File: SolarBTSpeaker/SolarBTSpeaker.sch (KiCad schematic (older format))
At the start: 27 parts

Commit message: Schematic updated
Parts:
- removed U?: LM2623AMM_NOPB, MUA08A, symbol LM2623:LM2623AMM_NOPB
- added C1, C10, C12, C16, C18: 0.1u, symbol Device:C_Small
- added C11, C13, C14, C17, C23, C24, C31, C32, C6, C7: 1000p, symbol Device:C_Small
- added C15, C9: 100u, symbol Device:CP1_Small
- added C19, C21, C25, C27: 0.22u, symbol Device:C_Small
- added C20, C22, C26, C29, C30, C33: 1u, symbol Device:C_Small
- added C28: 300u, symbol Device:CP1_Small
- added C8: 68u, symbol Device:CP1_Small
- added D4: 1N5822, Diode_THT:D_DO-201AD_P15.24mm_Horizontal, symbol Diode:1N5822
- added FB1, FB2, FB3, FB4: Ferrite_Bead_Small, symbol Device:Ferrite_Bead_Small
- added J10: IN_LEFT-, symbol Connector_Generic:Conn_01x01
- added J11: OUT_RIGHT-, symbol Connector_Generic:Conn_01x01
- added J12: IN_RIGHT-, symbol Connector_Generic:Conn_01x01
- added J13: OUT_RIGHT+, symbol Connector_Generic:Conn_01x01
- added J14: IN_RIGHT+, symbol Connector_Generic:Conn_01x01
- added J15: GAIN_Jumper, symbol Connector_Generic:Conn_01x03
- added J16, J17: Conn_01x01, symbol Connector_Generic:Conn_01x01
- added J7: OUT_LEFT+, symbol Connector_Generic:Conn_01x01
- added J8: OUT_LEFT-, symbol Connector_Generic:Conn_01x01
- added J9: IN_LEFT+, symbol Connector_Generic:Conn_01x01
- added L1: 22u, symbol Device:L
- added R1: 330, symbol Device:R_Small_US
- added R10, R11, R14, R9: 68, symbol Device:R_Small_US
- added R12, R13: 100k, symbol Device:R_Small_US
- added R15: 39k, symbol Device:R_Small_US
- added R2, R6: 5.1M, symbol Device:R_Small_US
- added R3: 2.2k, symbol Device:R_Small_US
- added Rsense1: 20m, symbol Device:R_Small_US
- added SW2: SW_SPDT, symbol Switch:SW_SPDT
- added TP4, TP5, TP6: TestPoint, symbol Connector:TestPoint
- added U3, U4: CSD16404Q5A, DQJ8, symbol CSD16404Q5A:CSD16404Q5A
- added U5: SIRA18ADP, symbol SolarBTSpeakerLib:SIRA18ADP
- added U6: max1771cpa+, 21-0043D_8, symbol MAX1771CPA+:max1771cpa+
- Rtherm1: renamed from R?; value 1M -> 21.5k
- SW1: renamed from SW?; value SW_DPDT_x2 -> SW_Input
- gave numbers to parts that had none: 23
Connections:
- net GND: now also U7.14 (AGND), U7.19 (GND), U7.24 (GND), U7.29 (PAD), U7.6 (MODE_SEL), U7.8 (GND), C10.2, C11.2, C12.2, C13.2, C15.2, C16.2, C17.2, C18.2, C20.2, C23.2, C28.2, C31.2, C33.2, C6.2, C8.2, C9.2, J15.1 (Pin_1), R10.2, R11.2, R14.2, R15.1, R3.2, R6.2, R9.2, Rsense1.2, U4.1 (S), U6.3 (FB), U6.4 (SHDN), U6.6 (AGND), U6.7 (GND)
- net at U7.10 (PLIMIT): now also U7.9 (GVDD), C33.1, R15.2
- net at U7.11 (RINN): now also C29.1
- net at U7.12 (RINP): now also C30.1
- net +12V: now reaches U7.15 (PVCC)
- net +12V: now also U7.16 (PVCC), U7.27 (PVCC), U7.28 (PVCC), U7.7 (AVCC), C10.1, C11.1, C12.1, C15.1, C16.1, C17.1, C20.1, C28.1, C9.1, D4.1 (K), R12.2, R13.2, TP4.1, TP5.1, TP6.1, U6.2 (V+)
- net at U7.17 (BSPR): now also C27.2
- net at U7.18 (OUTPR): now also C27.1, FB4.2
- net at U7.2 (SDZ_FAULT_N): now also R12.1
- net at U7.20 (OUTNR): now also C25.1, FB3.2
- net at U7.21 (BSNR): now also C25.2
- net at U7.22 (BSNL): now also C21.2
- net at U7.23 (OUTNL): now also C21.1, FB2.2
- net at U7.25 (OUTPL): now also C19.1, FB1.2
- net at U7.26 (BSPL): now also C19.2
- net at U7.3 (LINP): now also C22.1
- net at U7.4 (LINN): now also C26.1
- net at U7.5 (GAIN_SEL): now also J15.2 (Pin_2)
- net at U2.2 (COUT): now also R6.1, U4.2 (G)
- net at U2.3 (DOUT): now also R2.1, U3.2 (G)
- net at U2.4 (VSS): now also C1.2, J17.1 (Pin_1), R2.2, U3.1 (S)
- net at U2.5 (BAT): now also C1.1, R1.2
- net at U2.6 (V-): now also R3.1
- net BAT+: now reaches C4.1, C5.1, TP3.1, U1.10 (BAT)
- net BAT+: now also R7.2, R8.2, J16.1 (Pin_1), R1.1, SW2.2 (B)
- new net: U3.3 (D), U4.3 (D)
- new net: U5.4 (G), U6.1 (EXT)
- new net: C18.1, U6.5 (REF)
- new net: Rsense1.1, U5.1 (S), U5.2 (S), U5.3 (S), U6.8 (CS)
- new net: C8.1, L1.1, SW2.1 (A)
- new net: D4.2 (A), L1.2, U5.5 (D)
- new net: C22.2, J9.1 (Pin_1)
- new net: C26.2, J10.1 (Pin_1)
- new net: C29.2, J12.1 (Pin_1)
- new net: C30.2, J14.1 (Pin_1)
- new net: C6.1, C7.1, FB1.1, J7.1 (Pin_1)
- new net: C7.2, R9.1
- new net: C13.1, C14.1, FB2.1, J8.1 (Pin_1)
- new net: C14.2, R10.1
- new net: C23.1, C24.1, FB3.1, J11.1 (Pin_1)
- new net: C24.2, R11.1
- new net: C31.1, C32.1, FB4.1, J13.1 (Pin_1)
- new net: C32.2, R14.1
- new net: J15.3 (Pin_3), R13.1
- no-connect marks 1 -> 4
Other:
- note added: "Amplifier"
- note added: "Batt Input"
- note added: "Battery Charger"
- note added: "Battery Protection"
- note added: "DC-DC Boost Controller (12V Output)"
- note added: "Vin"
- note added: "Vout"
- moved on the sheet: C2, C3, C4, C5, D1, D2, D3, J1, J2, J3, J4, J5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

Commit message: Minor schematic updates
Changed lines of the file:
@@
 Connection ~ 6850 1300
 Wire Wire Line
-	7300 1300 7650 1300
+	7300 1300 7350 1300
 Connection ~ 7300 1300
 Wire Wire Line
@@
 Wire Notes Line
 	1800 7100 6700 7100
+Connection ~ 7350 1300
+Wire Wire Line
+	7350 1300 7650 1300
 $EndSCHEMATC

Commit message: Schematic Update
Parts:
- removed D1: D_Schottky, symbol Device:D_Schottky
- added C29: 150u, symbol Device:CP1_Small
- added D1: 1N5822, Diode_THT:D_DO-201AD_P15.24mm_Horizontal, symbol Diode:1N5822
- C1, C10, C11, C12, C13, C14, C16, C17, C18, C19, C2, C20, C21, C22, C23, C24, C25, C26, C27, C3, C4, C5, C6, C7: footprint (none) -> Capacitor_SMD:C_0805_2012Metric_Pad1.15x1.40mm_HandSolder
- C15, C8, C9: footprint (none) -> Capacitor_THT:CP_Radial_D6.3mm_P2.50mm
- C28: value 300u -> 150u
- C30: renamed from C29; footprint (none) -> Capacitor_SMD:C_0805_2012Metric_Pad1.15x1.40mm_HandSolder
- C31: renamed from C30; footprint (none) -> Capacitor_SMD:C_0805_2012Metric_Pad1.15x1.40mm_HandSolder
- C32: renamed from C31; footprint (none) -> Capacitor_SMD:C_0805_2012Metric_Pad1.15x1.40mm_HandSolder
- C33: renamed from C32; footprint (none) -> Capacitor_SMD:C_0805_2012Metric_Pad1.15x1.40mm_HandSolder
- C34: renamed from C33; footprint (none) -> Capacitor_SMD:C_0805_2012Metric_Pad1.15x1.40mm_HandSolder
- FB1, FB2, FB3, FB4, R1, R10, R11, R12, R13, R14, R15, R2, R3, R4, R5, R6, R7, R8, R9, Rsense1, Rtherm1: footprint (none) -> Resistor_SMD:R_0805_2012Metric_Pad1.15x1.40mm_HandSolder
- J1: renamed from J16; footprint (none) -> Connector_Wire:SolderWirePad_1x01_Drill1.5mm
- J10: renamed from J8; footprint (none) -> Connector_Wire:SolderWirePad_1x01_Drill1.5mm
- J11: renamed from J9; footprint (none) -> Connector_Wire:SolderWirePad_1x01_Drill1.5mm
- J12: renamed from J10; footprint (none) -> Connector_Wire:SolderWirePad_1x01_Drill1.5mm
- J13: renamed from J11; footprint (none) -> Connector_Wire:SolderWirePad_1x01_Drill1.5mm
- J14: renamed from J12; footprint (none) -> Connector_Wire:SolderWirePad_1x01_Drill1.5mm
- J15: renamed from J13; footprint (none) -> Connector_Wire:SolderWirePad_1x01_Drill1.5mm
- J16: renamed from J14; footprint (none) -> Connector_Wire:SolderWirePad_1x01_Drill1.5mm
- J17: renamed from J15; footprint (none) -> Connector_PinSocket_2.54mm:PinSocket_1x03_P2.54mm_Vertical
- J2: renamed from J17; footprint (none) -> Connector_Wire:SolderWirePad_1x01_Drill1.5mm
- J3: renamed from J1; footprint (none) -> Connector_Wire:SolderWirePad_1x01_Drill1.5mm
- J4: renamed from J2; footprint (none) -> Connector_Wire:SolderWirePad_1x01_Drill1.5mm
- J5: renamed from J3; footprint (none) -> Connector_Wire:SolderWirePad_1x01_Drill1.5mm
- J6: renamed from J4; footprint (none) -> Connector_Wire:SolderWirePad_1x01_Drill1.5mm
- J7: renamed from J5; footprint (none) -> Connector_Wire:SolderWirePad_1x01_Drill1.5mm
- J8: renamed from J6; footprint (none) -> Connector_Wire:SolderWirePad_1x01_Drill1.5mm
- J9: renamed from J7; footprint (none) -> Connector_Wire:SolderWirePad_1x01_Drill1.5mm
- SW1: footprint (none) -> Button_Switch_THT:SW_CuK_JS202011CQN_DPDT_Straight
- TP1, TP2, TP3, TP4, TP5, TP6: footprint (none) -> TestPoint:TestPoint_Pad_D1.0mm
- U1: footprint DQC10_P84X2P4 -> Package_SON:WSON-10-1EP_2x3mm_P0.5mm_EP0.84x2.4mm
- U2: footprint DSE0006A -> Package_SON:WSON-6_1.5x1.5mm_P0.5mm
- U3, U4: footprint DQJ8 -> Package_SON:VSONP-8-1EP_5x6_P1.27mm
- U5: footprint (none) -> Package_SO:PowerPAK_SO-8_Single
- U6: value max1771cpa+ -> max1771csa+; footprint 21-0043D_8 -> Package_SO:SOIC-8_3.9x4.9mm_P1.27mm
- U7: footprint PWP0028H_N -> Package_SO:HTSSOP-28-1EP_4.4x9.7mm_P0.65mm_EP2.85x5.4mm
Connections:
- net +12V: now also C29.1
- net GND: now also C29.2
- net at J3.1 (Pin_1): now also D1.2 (A)
- net at SW1.3 (C): now also D1.1 (K)

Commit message: Updated schematic with datasheets, fixed ERC warnings
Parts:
- C28, C29: footprint (none) -> Capacitor_THT:CP_Radial_D6.3mm_P2.50mm
- D2, D3: footprint (none) -> LED_THT:LED_D3.0mm
- L1: footprint (none) -> Solar BT Speaker Footprints:L_Radial_D14.8mm_P12mm_Wurth
- SW2: footprint (none) -> Connector_PinSocket_2.54mm:PinSocket_1x03_P2.54mm_Vertical
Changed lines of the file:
@@
 F 0 "D2" V 6197 3228 50  0000 L CNN
 F 1 "LED" V 6288 3228 50  0000 L CNN
-F 2 "" H 6250 3150 50  0001 C CNN
+F 2 "LED_THT:LED_D3.0mm" H 6250 3150 50  0001 C CNN
 F 3 "~" H 6250 3150 50  0001 C CNN
 	1    6250 3150
@@
 F 0 "D3" V 6597 3228 50  0000 L CNN
 F 1 "LED" V 6688 3228 50  0000 L CNN
-F 2 "" H 6650 3150 50  0001 C CNN
+F 2 "LED_THT:LED_D3.0mm" H 6650 3150 50  0001 C CNN
 F 3 "~" H 6650 3150 50  0001 C CNN
 	1    6650 3150
@@
 F 1 "CSD16404Q5A" H 10450 3251 60  0000 C CNN
 F 2 "Package_SON:VSONP-8-1EP_5x6_P1.27mm" H 10450 3240 60  0001 C CNN
-F 3 "" H 9850 3100 60  0000 C CNN
+F 3 "http://www.ti.com/general/docs/suppproductinfo.tsp?distId=10&gotoUrl=http%3A%2F%2Fwww.ti.com%2Flit%2Fgpn%2Fcsd16404q5a" H 10450 3251 60  0001 C CNN
 	1    9550 3100
 	1    0    0    -1
@@
 F 1 "CSD16404Q5A" H 10450 2401 60  0000 C CNN
 F 2 "Package_SON:VSONP-8-1EP_5x6_P1.27mm" H 10450 2390 60  0001 C CNN
-F 3 "" H 9850 2250 60  0000 C CNN
+F 3 "http://www.ti.com/general/docs/suppproductinfo.tsp?distId=10&gotoUrl=http%3A%2F%2Fwww.ti.com%2Flit%2Fgpn%2Fcsd16404q5a" H 9850 2250 60  0001 C CNN
 	1    9550 2250
 	1    0    0    -1
@@
 F 1 "max1771csa+" H 2900 6581 60  0000 C CNN
 F 2 "Package_SO:SOIC-8_3.9x4.9mm_P1.27mm" H 2900 6590 60  0001 C CNN
-F 3 "" H 3550 6100 60  0000 C CNN
+F 3 "https://datasheets.maximintegrated.com/en/ds/MAX1771.pdf" H 2900 6581 60  0001 C CNN
 	1    1800 6050
 	1    0    0    -1
@@
 F 0 "L1" V 5140 4850 50  0000 C CNN
 F 1 "22u" V 5049 4850 50  0000 C CNN
-F 2 "" H 4950 4850 50  0001 C CNN
-F 3 "~" H 4950 4850 50  0001 C CNN
+F 2 "Solar BT Speaker Footprints:L_Radial_D14.8mm_P12mm_Wurth" H 4950 4850 50  0001 C CNN
+F 3 "https://www.we-online.de/katalog/datasheet/744750560220.pdf" H 4950 4850 50  0001 C CNN
 	1    4950 4850
 	0    -1   -1   0
 $EndComp
-$Comp
-L SolarBTSpeakerLib:SIRA18ADP U5
-U 1 1 5EADD78B
-P 3650 5700
-F 0 "U5" H 4550 5957 60  0000 C CNN
-F 1 "SIRA18ADP" H 4550 5851 60  0000 C CNN
-F 2 "Package_SO:PowerPAK_SO-8_Single" H 4550 5840 60  0001 C CNN
-F 3 "" H 3950 5700 60  0000 C CNN
-	1    3650 5700
-	1    0    0    -1
-$EndComp
-Wire Wire Line
-	3950 6000 3550 6000
-Wire Wire Line
-	3950 5700 3950 5800
-Connection ~ 3950 5800
-Wire Wire Line
-	3950 5800 3950 5900
-Wire Wire Line
-	5150 5700 5150 5800
-Connection ~ 5150 5800
-Wire Wire Line
-	5150 5800 5150 5900
-Connection ~ 5150 5900
-Wire Wire Line
-	5150 5900 5150 6000
 Wire Wire Line
 	3950 5900 3700 5900
 Wire Wire Line
 	3700 5900 3700 6300
-Connection ~ 3950 5900
 Wire Wire Line
 	3550 6300 3700 6300
@@
 F 1 "68u" H 4841 5005 50  0000 L CNN
 F 2 "Capacitor_THT:CP_Radial_D6.3mm_P2.50mm" H 4750 5050 50  0001 C CNN
-F 3 "~" H 4750 5050 50  0001 C CNN
+F 3 "https://b2b-api.panasonic.eu/file_stream/pids/fileversion/8157" H 4750 5050 50  0001 C CNN
 	1    4750 5050
 	1    0    0    -1
@@
 F 1 "1N5822" H 5400 5575 50  0000 C CNN
 F 2 "Diode_THT:D_DO-201AD_P15.24mm_Horizontal" H 5400 5525 50  0001 C CNN
-F 3 "http://www.vishay.com/docs/88526/1n5820.pdf" H 5400 5700 50  0001 C CNN
+F 3 "https://www.onsemi.com/pub/Collateral/1N5820-D.PDF" H 5400 5700 50  0001 C CNN
 	1    5400 5700
 	-1   0    0    1
@@
 F 0 "C28" H 4341 6596 50  0000 L CNN
 F 1 "150u" H 4341 6505 50  0000 L CNN
-F 2 "" H 4250 6550 50  0001 C CNN
-F 3 "~" H 4250 6550 50  0001 C CNN
+F 2 "Capacitor_THT:CP_Radial_D6.3mm_P2.50mm" H 4250 6550 50  0001 C CNN
+F 3 "https://www.we-online.de/katalog/datasheet/860020373008.pdf" H 4250 6550 50  0001 C CNN
 	1    4250 6550
 	1    0    0    -1
@@
 F 0 "SW2" H 4350 5235 50  0000 C CNN
 F 1 "SW_SPDT" H 4350 5144 50  0000 C CNN
-F 2 "" H 4350 4950 50  0001 C CNN
+F 2 "Connector_PinSocket_2.54mm:PinSocket_1x03_P2.54mm_Vertical" H 4350 4950 50  0001 C CNN
 F 3 "~" H 4350 4950 50  0001 C CNN
 	1    4350 4950
@@
 F 1 "100u" H 9441 5005 50  0000 L CNN
 F 2 "Capacitor_THT:CP_Radial_D6.3mm_P2.50mm" H 9350 5050 50  0001 C CNN
-F 3 "~" H 9350 5050 50  0001 C CNN
+F 3 "https://www.nichicon.co.jp/english/products/pdfs/e-ufw.pdf" H 9350 5050 50  0001 C CNN
 	1    9350 5050
 	1    0    0    -1
@@
 F 1 "100u" H 9441 5605 50  0000 L CNN
 F 2 "Capacitor_THT:CP_Radial_D6.3mm_P2.50mm" H 9350 5650 50  0001 C CNN
-F 3 "~" H 9350 5650 50  0001 C CNN
+F 3 "https://www.nichicon.co.jp/english/products/pdfs/e-ufw.pdf" H 9350 5650 50  0001 C CNN
 	1    9350 5650
 	1    0    0    -1
@@
 F 1 "Ferrite_Bead_Small" V 13204 4000 50  0000 C CNN
 F 2 "Resistor_SMD:R_0805_2012Metric_Pad1.15x1.40mm_HandSolder" V 13280 4000 50  0001 C CNN
-F 3 "~" H 13350 4000 50  0001 C CNN
+F 3 "https://www.murata.com/en-us/products/productdata/8796736815134/ENFJ0002.pdf" H 13350 4000 50  0001 C CNN
 	1    13350 4000
 	0    1    1    0
@@
 F 1 "Ferrite_Bead_Small" V 13204 5000 50  0000 C CNN
 F 2 "Resistor_SMD:R_0805_2012Metric_Pad1.15x1.40mm_HandSolder" V 13280 5000 50  0001 C CNN
-F 3 "~" H 13350 5000 50  0001 C CNN
+F 3 "https://www.murata.com/en-us/products/productdata/8796736815134/ENFJ0002.pdf" H 13350 5000 50  0001 C CNN
 	1    13350 5000
 	0    1    1    0
@@
 F 1 "Ferrite_Bead_Small" V 13204 6000 50  0000 C CNN
 F 2 "Resistor_SMD:R_0805_2012Metric_Pad1.15x1.40mm_HandSolder" V 13280 6000 50  0001 C CNN
-F 3 "~" H 13350 6000 50  0001 C CNN
+F 3 "https://www.murata.com/en-us/products/productdata/8796736815134/ENFJ0002.pdf" H 13350 6000 50  0001 C CNN
 	1    13350 6000
 	0    1    1    0
@@
 F 1 "Ferrite_Bead_Small" V 13204 7000 50  0000 C CNN
 F 2 "Resistor_SMD:R_0805_2012Metric_Pad1.15x1.40mm_HandSolder" V 13280 7000 50  0001 C CNN
-F 3 "~" H 13350 7000 50  0001 C CNN
+F 3 "https://www.murata.com/en-us/products/productdata/8796736815134/ENFJ0002.pdf" H 13350 7000 50  0001 C CNN
 	1    13350 7000
 	0    1    1    0
@@
 F 0 "C29" H 4691 6596 50  0000 L CNN
 F 1 "150u" H 4691 6505 50  0000 L CNN
-F 2 "" H 4600 6550 50  0001 C CNN
-F 3 "~" H 4600 6550 50  0001 C CNN
+F 2 "Capacitor_THT:CP_Radial_D6.3mm_P2.50mm" H 4600 6550 50  0001 C CNN
+F 3 "https://www.we-online.de/katalog/datasheet/860020373008.pdf" H 4600 6550 50  0001 C CNN
 	1    4600 6550
 	1    0    0    -1
@@
 	4600 6750 4250 6750
 Connection ~ 4250 6750
+$Comp
+L power:PWR_FLAG #FLG0101
+U 1 1 5F2B26A0
+P 9150 4900
+F 0 "#FLG0101" H 9150 4975 50  0001 C CNN
+F 1 "PWR_FLAG" H 9150 5073 50  0000 C CNN
+F 2 "" H 9150 4900 50  0001 C CNN
+F 3 "~" H 9150 4900 50  0001 C CNN
+	1    9150 4900
+	1    0    0    -1
+$EndComp
+$Comp
+L power:PWR_FLAG #FLG0102
+U 1 1 5F2B355B
+P 6250 1850
+F 0 "#FLG0102" H 6250 1925 50  0001 C CNN
+F 1 "PWR_FLAG" H 6250 2023 50  0000 C CNN
+F 2 "" H 6250 1850 50  0001 C CNN
+F 3 "~" H 6250 1850 50  0001 C CNN
+	1    6250 1850
+	1    0    0    -1
+$EndComp
+Connection ~ 6250 1850
+$Comp
+L power:PWR_FLAG #FLG0103
+U 1 1 5F2B414C
+P 11450 1450
+F 0 "#FLG0103" H 11450 1525 50  0001 C CNN
+F 1 "PWR_FLAG" H 11450 1623 50  0000 C CNN
+F 2 "" H 11450 1450 50  0001 C CNN
+F 3 "~" H 11450 1450 50  0001 C CNN
+	1    11450 1450
+	1    0    0    -1
+$EndComp
+Connection ~ 11450 1450
+$Comp
+L power:PWR_FLAG #FLG0105
+U 1 1 5F2CB6DA
+P 10850 1300
+F 0 "#FLG0105" H 10850 1375 50  0001 C CNN
+F 1 "PWR_FLAG" H 10850 1473 50  0000 C CNN
+F 2 "" H 10850 1300 50  0001 C CNN
+F 3 "~" H 10850 1300 50  0001 C CNN
+	1    10850 1300
+	1    0    0    -1
+$EndComp
+Connection ~ 10850 1300
+Connection ~ 3950 5900
+Wire Wire Line
+	5150 5900 5150 6000
+Connection ~ 5150 5900
+Connection ~ 5150 5800
+Wire Wire Line
+	5150 5800 5150 5900
+Wire Wire Line
+	5150 5700 5150 5800
+Connection ~ 3950 5800
+Wire Wire Line
+	3950 5800 3950 5900
+Wire Wire Line
+	3950 5700 3950 5800
+Wire Wire Line
+	3950 6000 3550 6000
+$Comp
+L SolarBTSpeakerLib:SIRA18ADP U5
+U 1 1 5EADD78B
+P 3650 5700
+F 0 "U5" H 4550 5957 60  0000 C CNN
+F 1 "SIRA18ADP" H 4550 5851 60  0000 C CNN
+F 2 "Package_SO:PowerPAK_SO-8_Single" H 4550 5840 60  0001 C CNN
+F 3 "http://www.vishay.com/docs/65314/sira18adp.pdf" H 3950 5700 60  0001 C CNN
+	1    3650 5700
+	1    0    0    -1
+$EndComp
 $EndSCHEMATC

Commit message: PCB and schematic significantly updated
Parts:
- removed TP2, TP5: TestPoint, TestPoint:TestPoint_Pad_D1.0mm, symbol Connector:TestPoint
- added TP3: COUT, TestPoint:TestPoint_Pad_D1.5mm, symbol Connector:TestPoint
- added TP6: EXT, TestPoint:TestPoint_Pad_D1.5mm, symbol Connector:TestPoint
- J1: value Conn_01x01 -> BAT+
- J10: value OUT_LEFT- -> OUTL-
- J11: value IN_LEFT+ -> LIN+
- J12: value IN_LEFT- -> LIN-
- J13: value OUT_RIGHT- -> OUTR-
- J14: value IN_RIGHT- -> RIN-
- J15: value OUT_RIGHT+ -> OUTR+
- J16: value IN_RIGHT+ -> RIN+
- J2: value Conn_01x01 -> BAT-
- J3: value Conn_01x01 -> SlrPnl+
- J4: value Conn_01x01 -> SlrPnl-
- J5: value Conn_01x01 -> USB+
- J6: value Conn_01x01 -> USB-
- J7, J8: value Conn_01x01 -> ThmCpl
- J9: value OUT_LEFT+ -> OUTL+
- SW1: value SW_Input -> SW_Power
- SW2: value SW_SPDT -> SW_AMP
- TP1: value TestPoint -> VBUS; footprint TestPoint:TestPoint_Pad_D1.0mm -> TestPoint:TestPoint_Pad_D1.5mm
- TP2: renamed from TP3; value TestPoint -> BAT; footprint TestPoint:TestPoint_Pad_D1.0mm -> TestPoint:TestPoint_Pad_D1.5mm
- TP4: value TestPoint -> DOUT; footprint TestPoint:TestPoint_Pad_D1.0mm -> TestPoint:TestPoint_Pad_D1.5mm
- TP5: renamed from TP6; value TestPoint -> 12V; footprint TestPoint:TestPoint_Pad_D1.0mm -> TestPoint:TestPoint_Pad_D1.5mm
- renumbered Rtherm1 to Rth1
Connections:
- net +12V: no longer TP4.1
- net at R6.1, U2.2 (COUT), U4.2 (G): now also TP3.1
- net at R2.1, U2.3 (DOUT), U3.2 (G): now also TP4.1
- net at U5.4 (G), U6.1 (EXT): now also TP6.1

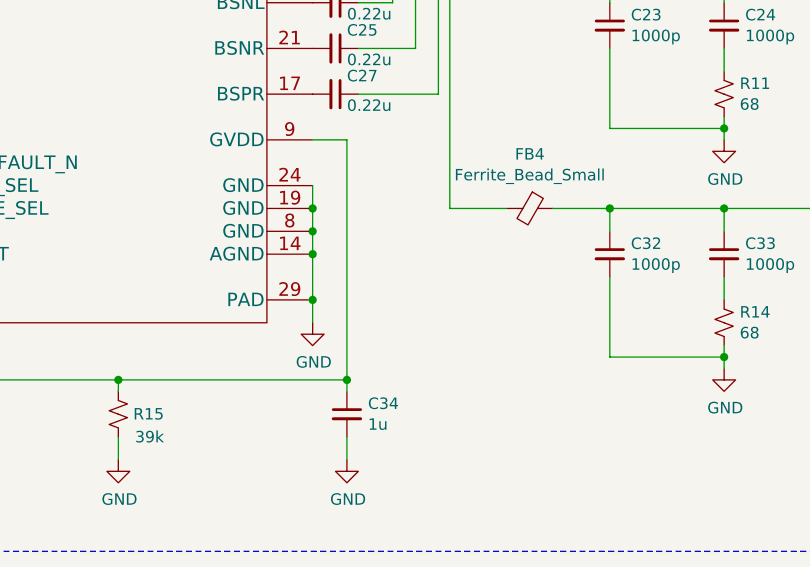
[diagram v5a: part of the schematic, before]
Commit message: Schematic and PCB finalized, gerbers and drill plot created
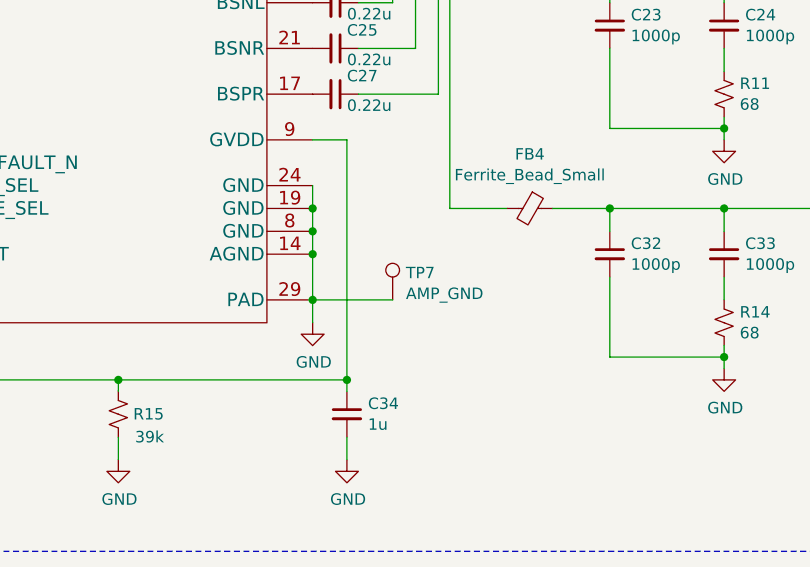
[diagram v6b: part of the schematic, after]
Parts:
- added TP7: AMP_GND, TestPoint:TestPoint_Pad_D1.5mm, symbol Connector:TestPoint
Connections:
- net GND: now also TP7.1
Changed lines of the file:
@@
 Wire Wire Line
 	10250 4900 10600 4900
+Wire Wire Line
+	12400 7400 12750 7400
+$Comp
+L Connector:TestPoint TP7
+U 1 1 5EE69FE9
+P 12750 7400
+F 0 "TP7" H 12808 7518 50  0000 L CNN
+F 1 "AMP_GND" H 12808 7427 50  0000 L CNN
+F 2 "TestPoint:TestPoint_Pad_D1.5mm" H 12950 7400 50  0001 C CNN
+F 3 "~" H 12950 7400 50  0001 C CNN
+	1    12750 7400
+	1    0    0    -1
+$EndComp
 $EndSCHEMATC
